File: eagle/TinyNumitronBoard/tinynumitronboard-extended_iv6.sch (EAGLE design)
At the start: 37 parts, among them IC1 IC_TD62783-SO-18W

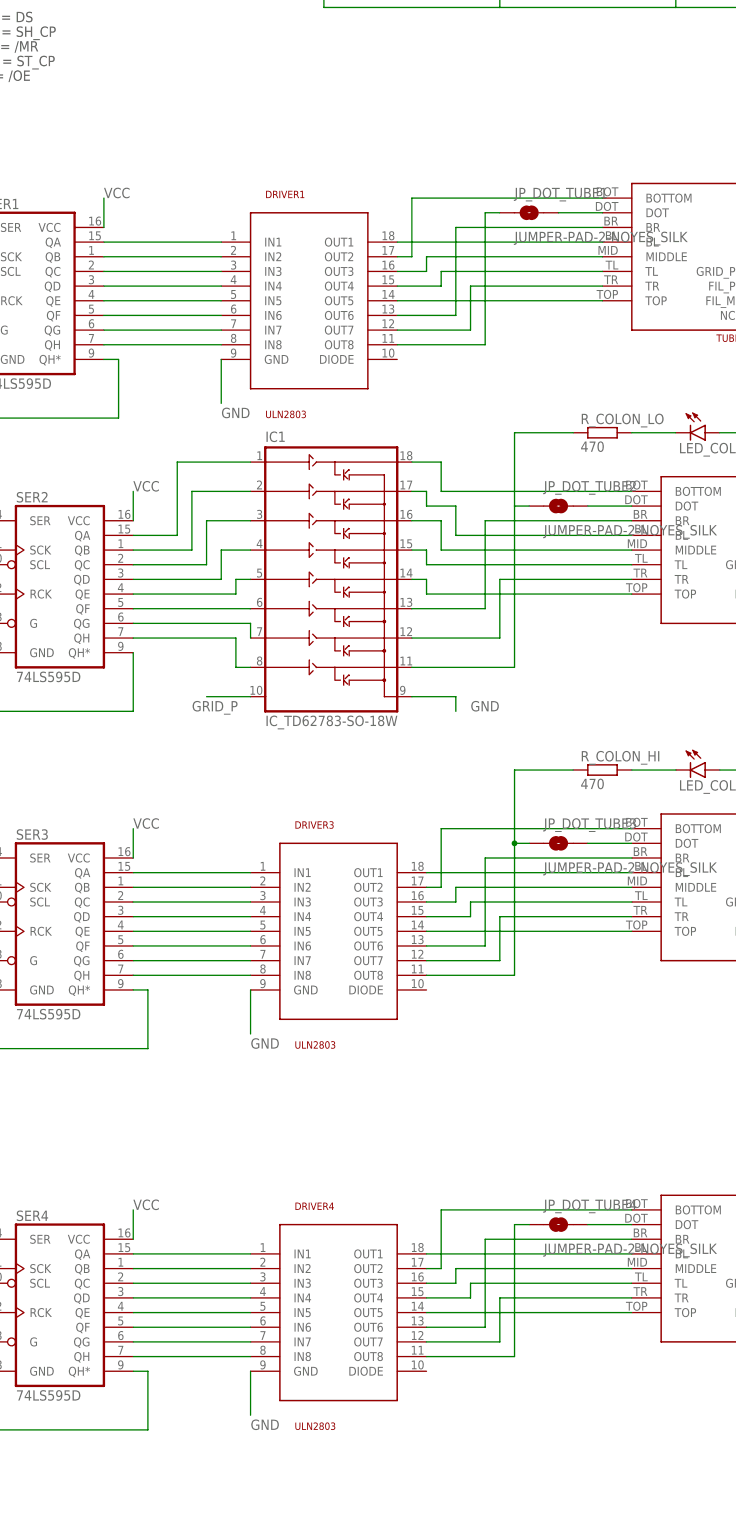
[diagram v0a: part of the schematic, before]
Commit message: Schematic fixed, placement done
Need to do routing now
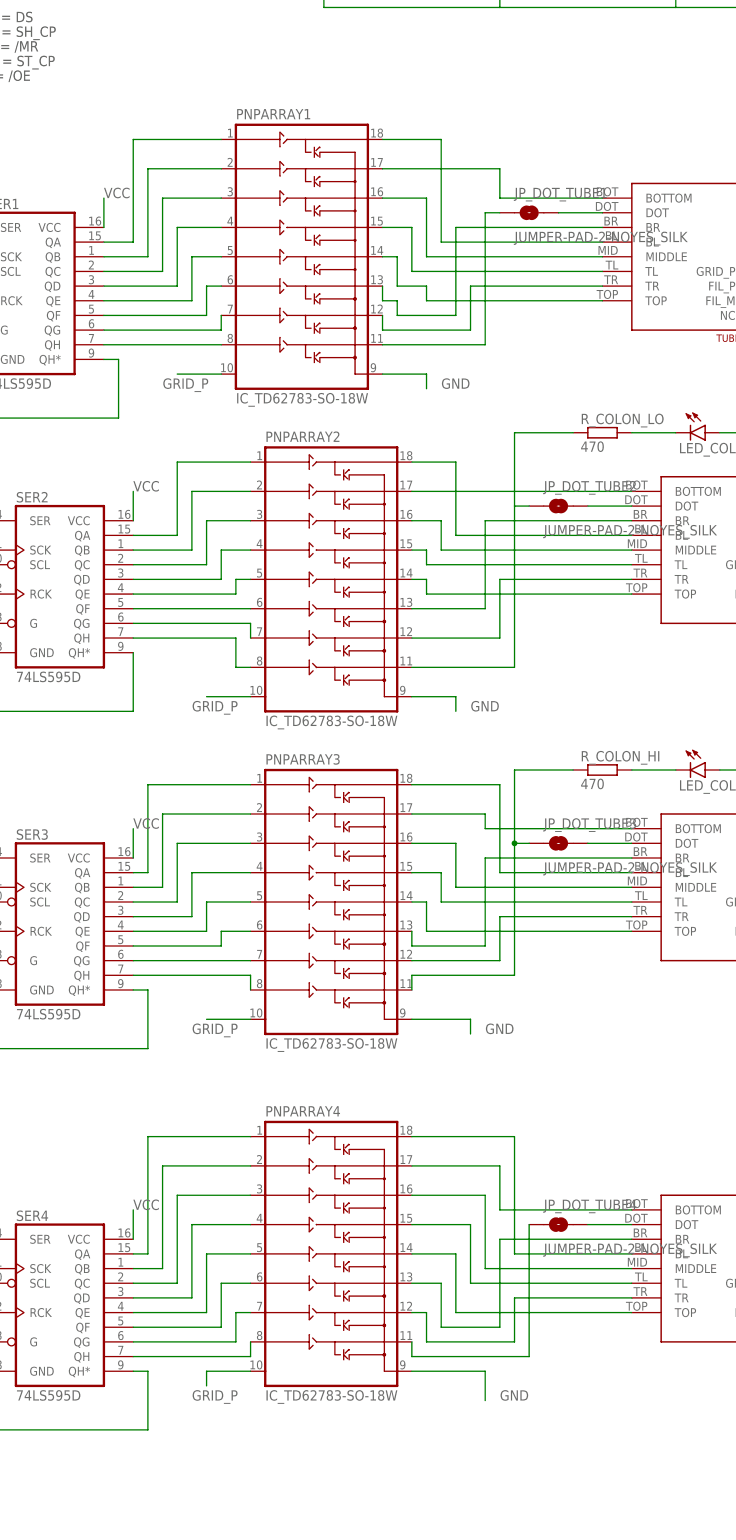
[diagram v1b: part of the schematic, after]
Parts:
- removed DRIVER1, DRIVER3, DRIVER4: ULN2803, uln2803:ULN2803
- added PNPARRAY1, PNPARRAY3, PNPARRAY4: IC_TD62783-SO-18W, dp_devices:IC_TD62783-SO-18W
- renumbered IC1 to PNPARRAY2
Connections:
- net GND: now also PNPARRAY1.GND, PNPARRAY3.GND, PNPARRAY4.GND; no longer DRIVER1.GND, DRIVER3.GND, DRIVER4.GND
- net GRID_P: now also PNPARRAY1.VS, PNPARRAY3.VS, PNPARRAY4.VS
- net N$1: now also PNPARRAY1.IN5, SER1.QE; no longer DRIVER1.IN1, SER1.QA
- net N$14: now also PNPARRAY2.OUT1; no longer PNPARRAY2.OUT2
- net N$15: now also PNPARRAY1.OUT1; no longer DRIVER1.OUT1
- net N$16: now also PNPARRAY2.OUT2; no longer PNPARRAY2.OUT1
- net N$18: now also PNPARRAY1.OUT2; no longer DRIVER1.OUT2
- net N$19: now also PNPARRAY1.OUT3; no longer DRIVER1.OUT3
- net N$2: now also PNPARRAY1.IN4, SER1.QD; no longer DRIVER1.IN2, SER1.QB
- net N$24: now also PNPARRAY4.OUT1; no longer DRIVER4.OUT1
- net N$25: now also PNPARRAY4.OUT2; no longer DRIVER4.OUT2
- net N$26: now also PNPARRAY4.OUT3; no longer DRIVER4.OUT3
- net N$27: now also PNPARRAY4.OUT4; no longer DRIVER4.OUT4
- net N$28: now also PNPARRAY4.OUT5; no longer DRIVER4.OUT5
- net N$29: now also PNPARRAY4.OUT6; no longer DRIVER4.OUT6
- net N$3: now also PNPARRAY1.IN3; no longer DRIVER1.IN3
- net N$30: now also PNPARRAY4.OUT7; no longer DRIVER4.OUT7
- net N$31: now also PNPARRAY4.OUT8; no longer DRIVER4.OUT8
- net N$32: now also PNPARRAY4.IN1; no longer DRIVER4.IN1
- net N$33: now also PNPARRAY4.IN2; no longer DRIVER4.IN2
- net N$34: now also PNPARRAY4.IN3; no longer DRIVER4.IN3
- net N$35: now also PNPARRAY4.IN4; no longer DRIVER4.IN4
- net N$36: now also PNPARRAY4.IN5; no longer DRIVER4.IN5
- net N$37: now also PNPARRAY4.IN6; no longer DRIVER4.IN6
- net N$38: now also PNPARRAY1.OUT4; no longer DRIVER1.OUT4
- net N$4: now also PNPARRAY1.IN2, SER1.QB; no longer DRIVER1.IN4, SER1.QD
- net N$5: now also PNPARRAY1.IN1, SER1.QA; no longer DRIVER1.IN5, SER1.QE
- net N$52: now also PNPARRAY4.IN7; no longer DRIVER4.IN7
- net N$54: now also PNPARRAY3.OUT1; no longer DRIVER3.OUT1
- net N$55: now also PNPARRAY1.OUT5; no longer DRIVER1.OUT5
- net N$56: now also PNPARRAY1.OUT6; no longer DRIVER1.OUT6
- net N$57: now also PNPARRAY1.OUT7; no longer DRIVER1.OUT7
- net N$58: now also PNPARRAY3.OUT2; no longer DRIVER3.OUT2
- net N$59: now also PNPARRAY1.OUT8; no longer DRIVER1.OUT8
- net N$6: now also PNPARRAY1.IN6; no longer DRIVER1.IN6
- net N$60: now also PNPARRAY3.OUT3; no longer DRIVER3.OUT3
- net N$61: now also PNPARRAY3.OUT4; no longer DRIVER3.OUT4
- net N$62: now also PNPARRAY3.OUT5; no longer DRIVER3.OUT5
- net N$63: now also PNPARRAY3.OUT6; no longer DRIVER3.OUT6
- net N$64: now also PNPARRAY3.OUT7; no longer DRIVER3.OUT7
- net N$65: now also PNPARRAY3.OUT8; no longer DRIVER3.OUT8
- net N$66: now also PNPARRAY3.IN1; no longer DRIVER3.IN1
- net N$67: now also PNPARRAY3.IN2; no longer DRIVER3.IN2
- net N$68: now also PNPARRAY3.IN3; no longer DRIVER3.IN3
- net N$69: now also PNPARRAY3.IN4; no longer DRIVER3.IN4
- net N$7: now also PNPARRAY1.IN7; no longer DRIVER1.IN7
- net N$70: now also PNPARRAY3.IN5; no longer DRIVER3.IN5
- net N$71: now also PNPARRAY3.IN6; no longer DRIVER3.IN6
- net N$72: now also PNPARRAY3.IN7; no longer DRIVER3.IN7
- net N$73: now also PNPARRAY3.IN8; no longer DRIVER3.IN8
- net N$74: now also PNPARRAY4.IN8; no longer DRIVER4.IN8
- net N$8: now also PNPARRAY1.IN8; no longer DRIVER1.IN8

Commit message: Manual wiring WiP (30%)
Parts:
- removed FILGND2GND: JUMPER-PAD-2-NOYES_SILK, SparkFun-Passives:JUMPER-PAD-2-NOYES_SILK
- removed J_TUBEPOWER_IN, J_TUBEPOWER_OUT: (no value), SparkFun-Connectors:M03LOCK
- added J1, J2: (no value), SparkFun-Connectors:CONN_021X02_NO_SILK
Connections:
- removed net FIL_M: FILGND2GND.1, J_TUBEPOWER_IN.3, J_TUBEPOWER_OUT.3, TUBE1.FIL_M, TUBE2.FIL_M, TUBE3.FIL_M, TUBE4.FIL_M
- net FIL_P: now also J1.2, J2.2; no longer J_TUBEPOWER_IN.2, J_TUBEPOWER_OUT.2
- net GND: now also TUBE1.FIL_M, TUBE2.FIL_M, TUBE3.FIL_M, TUBE4.FIL_M; no longer FILGND2GND.2
- net GRID_P: now also J1.1, J2.1; no longer J_TUBEPOWER_IN.1, J_TUBEPOWER_OUT.1
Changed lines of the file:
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@@
 <part name="TUBE4" library="kalshagar" deviceset="IV6_NUMITRON" device="LARGE" value="IV6_NUMITRONLARGE"/>
 <part name="SER4" library="SparkFun-DigitalIC" deviceset="74*595" device="D" technology="LS"/>
-<part name="J_TUBEPOWER_IN" library="SparkFun-Connectors" deviceset="M03" device="LOCK"/>
-<part name="J_TUBEPOWER_OUT" library="SparkFun-Connectors" deviceset="M03" device="LOCK"/>
-<part name="FILGND2GND" library="SparkFun-Passives" deviceset="JUMPER-PAD-2-NO" device="YES_SILK"/>
 <part name="C2" library="SparkFun-Passives" deviceset="CAP_POL" device="D"/>
 <part name="LED_COLON_LO" library="SparkFun-LED" deviceset="LED" device="1206"/>
@@
 <part name="PNPARRAY3" library="dp_devices" deviceset="IC_TD62783" device="-SO-18W"/>
 <part name="PNPARRAY4" library="dp_devices" deviceset="IC_TD62783" device="-SO-18W"/>
+<part name="J1" library="SparkFun-Connectors" deviceset="CONN_02" device="1X02_NO_SILK"/>
+<part name="J2" library="SparkFun-Connectors" deviceset="CONN_02" device="1X02_NO_SILK"/>
 </parts>
 <sheets>
@@
 <instance part="TUBE4" gate="G$1" x="71.12" y="-116.84" rot="R180"/>
 <instance part="SER4" gate="A" x="-45.72" y="-121.92"/>
-<instance part="J_TUBEPOWER_IN" gate="J$1" x="114.3" y="86.36" rot="R270"/>
-<instance part="J_TUBEPOWER_OUT" gate="J$1" x="114.3" y="-144.78" rot="R270"/>
-<instance part="FILGND2GND" gate="G$1" x="124.46" y="60.96"/>
 <instance part="C2" gate="G$1" x="-119.38" y="45.72"/>
 <instance part="LED_COLON_LO" gate="G$1" x="68.58" y="27.94" rot="R270"/>
@@
 <instance part="PNPARRAY3" gate="IC" x="2.54" y="-53.34"/>
 <instance part="PNPARRAY4" gate="IC" x="2.54" y="-114.3"/>
+<instance part="J1" gate="G$1" x="111.76" y="86.36" rot="R270"/>
+<instance part="J2" gate="G$1" x="111.76" y="-144.78" rot="R270"/>
 </instances>
 <busses>
@@
 </segment>
 <segment>
-<pinref part="FILGND2GND" gate="G$1" pin="2"/>
-<wire x1="129.54" y1="60.96" x2="132.08" y2="60.96" width="0.1524" layer="91"/>
-<wire x1="132.08" y1="60.96" x2="132.08" y2="53.34" width="0.1524" layer="91"/>
-<label x="132.08" y="50.8" size="1.778" layer="95"/>
-</segment>
-<segment>
 <pinref part="PNPARRAY2" gate="IC" pin="GND"/>
 <wire x1="17.78" y1="-17.78" x2="25.4" y2="-17.78" width="0.1524" layer="91"/>
@@
 <wire x1="30.48" y1="-134.62" x2="30.48" y2="-139.7" width="0.1524" layer="91"/>
 <label x="33.02" y="-139.7" size="1.778" layer="95"/>
+</segment>
+<segment>
+<pinref part="TUBE1" gate="G$1" pin="FIL_M"/>
+<wire x1="116.84" y1="-124.46" x2="116.84" y2="-58.42" width="0.1524" layer="91"/>
+<wire x1="116.84" y1="-58.42" x2="116.84" y2="0" width="0.1524" layer="91"/>
+<wire x1="116.84" y1="0" x2="116.84" y2="50.8" width="0.1524" layer="91"/>
+<wire x1="116.84" y1="50.8" x2="116.84" y2="60.96" width="0.1524" layer="91"/>
+<wire x1="81.28" y1="50.8" x2="116.84" y2="50.8" width="0.1524" layer="91"/>
+<junction x="116.84" y="50.8"/>
+<pinref part="TUBE2" gate="G$1" pin="FIL_M"/>
+<wire x1="86.36" y1="0" x2="116.84" y2="0" width="0.1524" layer="91"/>
+<pinref part="TUBE3" gate="G$1" pin="FIL_M"/>
+<wire x1="86.36" y1="-58.42" x2="116.84" y2="-58.42" width="0.1524" layer="91"/>
+<pinref part="TUBE4" gate="G$1" pin="FIL_M"/>
+<wire x1="86.36" y1="-124.46" x2="116.84" y2="-124.46" width="0.1524" layer="91"/>
+<label x="119.38" y="53.34" size="1.778" layer="95" rot="R90"/>
+<wire x1="119.38" y1="60.96" x2="116.84" y2="60.96" width="0.1524" layer="91"/>
+<junction x="116.84" y="0"/>
+<junction x="116.84" y="-58.42"/>
 </segment>
 </net>
@@
 <net name="GRID_P" class="0">
 <segment>
-<pinref part="J_TUBEPOWER_IN" gate="J$1" pin="1"/>
-<pinref part="J_TUBEPOWER_OUT" gate="J$1" pin="1"/>
 <wire x1="111.76" y1="78.74" x2="111.76" y2="55.88" width="0.1524" layer="91"/>
 <pinref part="TUBE1" gate="G$1" pin="GRID_P"/>
@@
 <junction x="111.76" y="-53.34"/>
 <junction x="111.76" y="-119.38"/>
+<pinref part="J1" gate="G$1" pin="1"/>
+<pinref part="J2" gate="G$1" pin="1"/>
 </segment>
 <segment>
@@
 <net name="FIL_P" class="0">
 <segment>
-<pinref part="J_TUBEPOWER_IN" gate="J$1" pin="2"/>
-<pinref part="J_TUBEPOWER_OUT" gate="J$1" pin="2"/>
 <wire x1="114.3" y1="78.74" x2="114.3" y2="53.34" width="0.1524" layer="91"/>
 <pinref part="TUBE1" gate="G$1" pin="FIL_P"/>
@@
 <junction x="114.3" y="-55.88"/>
 <junction x="114.3" y="-121.92"/>
-</segment>
-</net>
-<net name="FIL_M" class="0">
-<segment>
-<pinref part="J_TUBEPOWER_OUT" gate="J$1" pin="3"/>
-<pinref part="J_TUBEPOWER_IN" gate="J$1" pin="3"/>
-<wire x1="116.84" y1="-152.4" x2="116.84" y2="-124.46" width="0.1524" layer="91"/>
-<pinref part="TUBE1" gate="G$1" pin="FIL_M"/>
-<wire x1="116.84" y1="-124.46" x2="116.84" y2="-58.42" width="0.1524" layer="91"/>
-<wire x1="116.84" y1="-58.42" x2="116.84" y2="0" width="0.1524" layer="91"/>
-<wire x1="116.84" y1="0" x2="116.84" y2="50.8" width="0.1524" layer="91"/>
-<wire x1="116.84" y1="50.8" x2="116.84" y2="60.96" width="0.1524" layer="91"/>
-<wire x1="116.84" y1="60.96" x2="116.84" y2="78.74" width="0.1524" layer="91"/>
-<wire x1="81.28" y1="50.8" x2="116.84" y2="50.8" width="0.1524" layer="91"/>
-<junction x="116.84" y="50.8"/>
-<pinref part="TUBE2" gate="G$1" pin="FIL_M"/>
-<wire x1="86.36" y1="0" x2="116.84" y2="0" width="0.1524" layer="91"/>
-<pinref part="TUBE3" gate="G$1" pin="FIL_M"/>
-<wire x1="86.36" y1="-58.42" x2="116.84" y2="-58.42" width="0.1524" layer="91"/>
-<pinref part="TUBE4" gate="G$1" pin="FIL_M"/>
-<wire x1="86.36" y1="-124.46" x2="116.84" y2="-124.46" width="0.1524" layer="91"/>
-<label x="116.84" y="68.58" size="1.778" layer="95" rot="R90"/>
-<pinref part="FILGND2GND" gate="G$1" pin="1"/>
-<wire x1="119.38" y1="60.96" x2="116.84" y2="60.96" width="0.1524" layer="91"/>
-<junction x="116.84" y="0"/>
-<junction x="116.84" y="-58.42"/>
-<junction x="116.84" y="-124.46"/>
-</segment>
-</net>
-<net name="N$20" class="0">
+<pinref part="J1" gate="G$1" pin="2"/>
+<pinref part="J2" gate="G$1" pin="2"/>
+</segment>
+</net>
+<net name="N$112" class="0">
 <segment>
 <pinref part="J_LED_OUT" gate="G$1" pin="1"/>

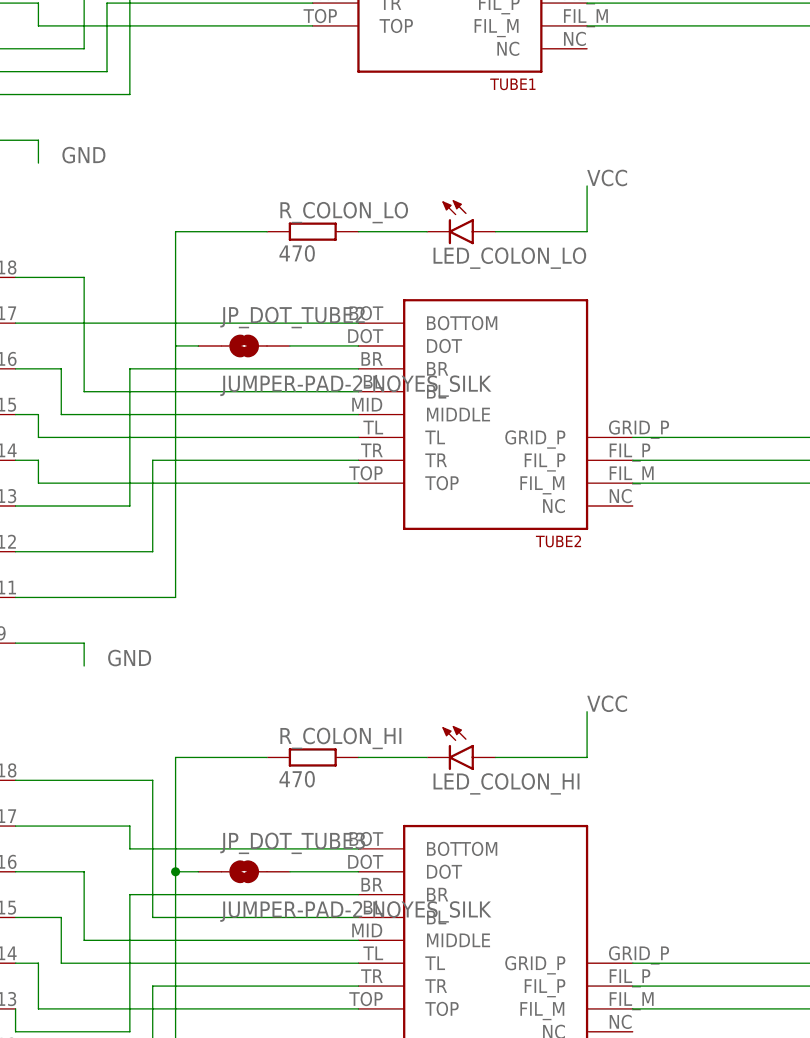
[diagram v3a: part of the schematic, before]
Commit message: Removed LEDs for colon
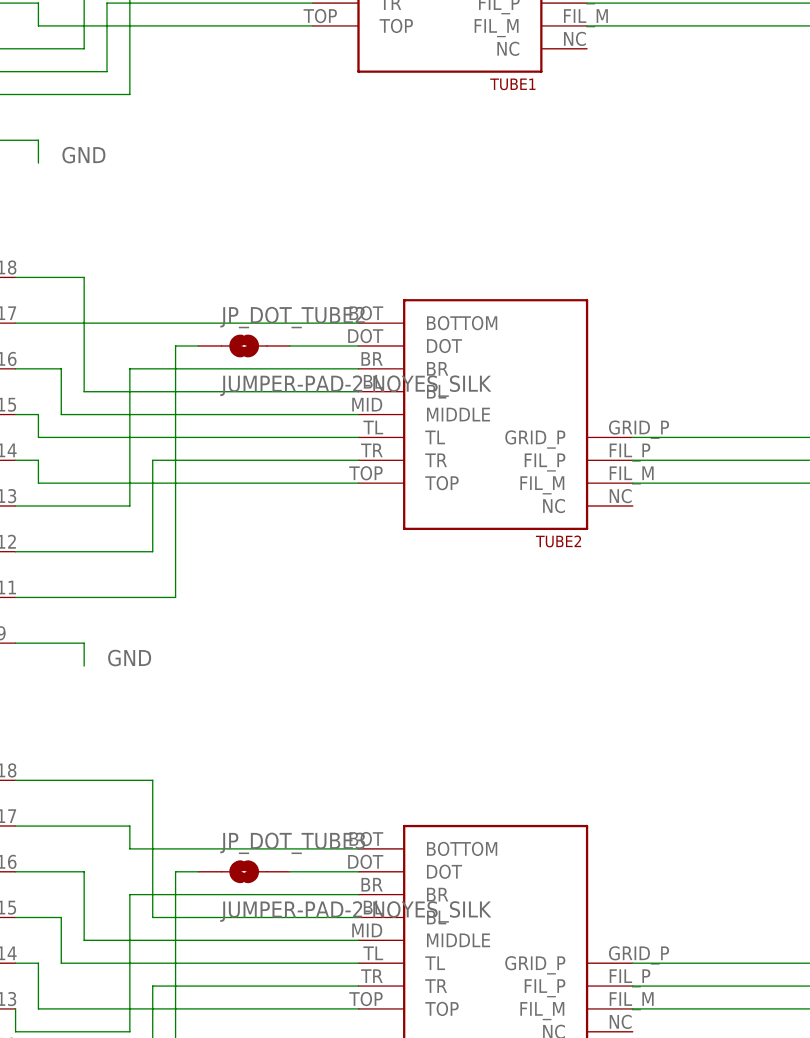
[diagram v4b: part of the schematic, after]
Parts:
- removed LED_COLON_HI, LED_COLON_LO: (no value), SparkFun-LED:LED1206
- removed R_COLON_HI, R_COLON_LO: 470, resistor:R-EU_M1206
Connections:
- removed net N$22: LED_COLON_LO.C, R_COLON_LO.2
- removed net N$77: LED_COLON_HI.C, R_COLON_HI.2
- net N$43: no longer R_COLON_LO.1
- net N$65: no longer R_COLON_HI.1
- net VCC: no longer LED_COLON_HI.A, LED_COLON_LO.A
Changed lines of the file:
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@@
 <part name="SER4" library="SparkFun-DigitalIC" deviceset="74*595" device="D" technology="LS"/>
 <part name="C2" library="SparkFun-Passives" deviceset="CAP_POL" device="D"/>
-<part name="LED_COLON_LO" library="SparkFun-LED" deviceset="LED" device="1206"/>
-<part name="R_COLON_LO" library="resistor" deviceset="R-EU_" device="M1206" value="470"/>
 <part name="JP_DOT_TUBE2" library="SparkFun-Passives" deviceset="JUMPER-PAD-2-NO" device="YES_SILK" value="JUMPER-PAD-2-NOYES_SILK"/>
-<part name="LED_COLON_HI" library="SparkFun-LED" deviceset="LED" device="1206"/>
-<part name="R_COLON_HI" library="resistor" deviceset="R-EU_" device="M1206" value="470"/>
 <part name="JP_DOT_TUBE3" library="SparkFun-Passives" deviceset="JUMPER-PAD-2-NO" device="YES_SILK" value="JUMPER-PAD-2-NOYES_SILK"/>
 <part name="JP_DOT_TUBE1" library="SparkFun-Passives" deviceset="JUMPER-PAD-2-NO" device="YES_SILK" value="JUMPER-PAD-2-NOYES_SILK"/>
@@
 <instance part="SER4" gate="A" x="-45.72" y="-121.92"/>
 <instance part="C2" gate="G$1" x="-119.38" y="45.72"/>
-<instance part="LED_COLON_LO" gate="G$1" x="68.58" y="27.94" rot="R270"/>
-<instance part="R_COLON_LO" gate="G$1" x="50.8" y="27.94"/>
 <instance part="JP_DOT_TUBE2" gate="G$1" x="43.18" y="15.24"/>
-<instance part="LED_COLON_HI" gate="G$1" x="68.58" y="-30.48" rot="R270"/>
-<instance part="R_COLON_HI" gate="G$1" x="50.8" y="-30.48"/>
 <instance part="JP_DOT_TUBE3" gate="G$1" x="43.18" y="-43.18"/>
 <instance part="JP_DOT_TUBE1" gate="G$1" x="38.1" y="66.04"/>
@@
 <wire x1="-60.96" y1="-119.38" x2="-55.88" y2="-119.38" width="0.1524" layer="91"/>
 <pinref part="SER4" gate="A" pin="SCL"/>
-</segment>
-<segment>
-<pinref part="LED_COLON_LO" gate="G$1" pin="A"/>
-<wire x1="71.12" y1="27.94" x2="81.28" y2="27.94" width="0.1524" layer="91"/>
-<wire x1="81.28" y1="27.94" x2="81.28" y2="33.02" width="0.1524" layer="91"/>
-<label x="81.28" y="33.02" size="1.778" layer="95"/>
-</segment>
-<segment>
-<pinref part="LED_COLON_HI" gate="G$1" pin="A"/>
-<wire x1="71.12" y1="-30.48" x2="81.28" y2="-30.48" width="0.1524" layer="91"/>
-<wire x1="81.28" y1="-30.48" x2="81.28" y2="-25.4" width="0.1524" layer="91"/>
-<label x="81.28" y="-25.4" size="1.778" layer="95"/>
 </segment>
 </net>
@@
 <wire x1="17.78" y1="-12.7" x2="35.56" y2="-12.7" width="0.1524" layer="91"/>
 <wire x1="35.56" y1="-12.7" x2="35.56" y2="15.24" width="0.1524" layer="91"/>
-<pinref part="R_COLON_LO" gate="G$1" pin="1"/>
-<wire x1="35.56" y1="15.24" x2="35.56" y2="27.94" width="0.1524" layer="91"/>
-<wire x1="45.72" y1="27.94" x2="35.56" y2="27.94" width="0.1524" layer="91"/>
 <pinref part="JP_DOT_TUBE2" gate="G$1" pin="1"/>
 <wire x1="38.1" y1="15.24" x2="35.56" y2="15.24" width="0.1524" layer="91"/>
@@
 <wire x1="17.78" y1="-66.04" x2="35.56" y2="-66.04" width="0.1524" layer="91"/>
 <wire x1="35.56" y1="-66.04" x2="35.56" y2="-43.18" width="0.1524" layer="91"/>
-<pinref part="R_COLON_HI" gate="G$1" pin="1"/>
-<wire x1="35.56" y1="-43.18" x2="35.56" y2="-30.48" width="0.1524" layer="91"/>
-<wire x1="45.72" y1="-30.48" x2="35.56" y2="-30.48" width="0.1524" layer="91"/>
 <pinref part="JP_DOT_TUBE3" gate="G$1" pin="1"/>
 <wire x1="38.1" y1="-43.18" x2="35.56" y2="-43.18" width="0.1524" layer="91"/>
-<junction x="35.56" y="-43.18"/>
 <pinref part="PNPARRAY3" gate="IC" pin="OUT8"/>
 <wire x1="17.78" y1="-66.04" x2="17.78" y2="-68.58" width="0.1524" layer="91"/>
@@
 </segment>
 </net>
-<net name="N$22" class="0">
-<segment>
-<pinref part="R_COLON_LO" gate="G$1" pin="2"/>
-<pinref part="LED_COLON_LO" gate="G$1" pin="C"/>
-<wire x1="55.88" y1="27.94" x2="63.5" y2="27.94" width="0.1524" layer="91"/>
-</segment>
-</net>
 <net name="N$75" class="0">
 <segment>
@@
 </segment>
 </net>
-<net name="N$77" class="0">
-<segment>
-<pinref part="R_COLON_HI" gate="G$1" pin="2"/>
-<pinref part="LED_COLON_HI" gate="G$1" pin="C"/>
-<wire x1="55.88" y1="-30.48" x2="63.5" y2="-30.48" width="0.1524" layer="91"/>
-</segment>
-</net>
